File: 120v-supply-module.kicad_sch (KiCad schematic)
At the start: 10 parts

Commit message: Place Holder:
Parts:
- removed U?: (no value), symbol Sensor_Current:ACS706xLC-05C
- added SW2: SW_DP3T, symbol Switch:SW_DP3T
- F2: value (none) -> Fuse
- J1: renamed from J?; value (none) -> VAC_GROUND_TERM
- J3: value (none) -> VAC_LIVE_TERM
- J4: value (none) -> VAC_NUETRAL_TERM
- K2: value (none) -> 12VDC SPDT Relay (240V 10A); footprint (none) -> Relay_THT:Relay_SPDT_RAYEX-L90S
- SW3: value (none) -> SW_SP3T
- SW4: value (none) -> SW_SPST
- T1: value (none) -> Transformer_1P_1S
- U1: value (none) -> AC PWM; footprint (none) -> Package_SO:SOIC-8_3.9x4.9mm_P1.27mm
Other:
- note added: "AC PWM Device"
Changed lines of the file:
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@@
     (effects (font (size 1.27 1.27)) (justify left bottom))
   )
-  (text "NOTE: ALL VAC IS UNPROTECTED BY THE POWER SUPPLY." (at 115.57 52.07 0)
+  (text "NOTE: ALL VAC IS UNPROTECTED BY THE POWER SUPPLY." (at 35.56 39.37 0)
     (effects (font (size 1.27 1.27) (thickness 0.254) bold) (justify left bottom))
   )
@@
     (effects (font (size 1.27 1.27)) (justify left bottom))
   )
-  (text "VAC_NUETRAL" (at 49.53 134.62 0)
+  (text "VAC_NUETRAL" (at 45.72 134.62 0)
     (effects (font (size 1.27 1.27)) (justify left bottom))
   )
@@
     (effects (font (size 1.27 1.27)) (justify left bottom))
   )
+  (text "AC PWM Device" (at 72.39 99.06 0)
+    (effects (font (size 1.27 1.27)) (justify left bottom))
+  )
   (text "120VAC_DIRECT_SUPPLY" (at 82.55 78.74 0)
     (effects (font (size 1.27 1.27)) (justify left bottom))
@@
       (effects (font (size 1.27 1.27)) (justify right))
     )
-    (property "Value" "" (id 1) (at 88.9 105.4099 0)
+    (property "Value" "AC PWM " (id 1) (at 88.9 105.4099 0)
       (effects (font (size 1.27 1.27)) (justify right))
     )
-    (property "Footprint" "" (id 2) (at 88.9 106.68 0)
+    (property "Footprint" "Package_SO:SOIC-8_3.9x4.9mm_P1.27mm" (id 2) (at 88.9 106.68 0)
       (effects (font (size 1.27 1.27) italic) (justify left) hide)
     )
@@
     (in_bom yes) (on_board yes) (fields_autoplaced)
     (property "Reference" "T1" (id 0) (at 72.4027 120.65 0))
-    (property "Value" "" (id 1) (at 72.4027 123.19 0))
+    (property "Value" "Transformer_1P_1S" (id 1) (at 72.4027 123.19 0))
     (property "Footprint" "" (id 2) (at 72.39 130.81 0)
       (effects (font (size 1.27 1.27)) hide)
@@
       (effects (font (size 1.27 1.27)) (justify left))
     )
-    (property "Value" "" (id 1) (at 205.74 100.3299 0)
+    (property "Value" "12VDC SPDT Relay (240V 10A)" (id 1) (at 205.74 100.3299 0)
       (effects (font (size 1.27 1.27)) (justify left))
     )
-    (property "Footprint" "" (id 2) (at 205.74 100.33 0)
+    (property "Footprint" "Relay_THT:Relay_SPDT_RAYEX-L90S" (id 2) (at 205.74 100.33 0)
       (effects (font (size 1.27 1.27)) (justify left) hide)
     )
@@
     (in_bom yes) (on_board yes)
     (property "Reference" "J3" (id 0) (at 28.575 73.66 0))
-    (property "Value" "" (id 1) (at 28.575 76.2 0))
+    (property "Value" "VAC_LIVE_TERM" (id 1) (at 28.575 76.2 0))
     (property "Footprint" "" (id 2) (at 27.94 78.74 0)
       (effects (font (size 1.27 1.27)) hide)
@@
     (pin "1")
   )
-  (symbol (lib_id "Switch:SW_SPST") (at 226.06 81.28 0) (unit 1)
-    (in_bom yes) (on_board yes) (fields_autoplaced)
-    (property "Reference" "SW4" (id 0) (at 226.06 74.93 0))
-    (property "Value" "" (id 1) (at 226.06 77.47 0))
-    (property "Footprint" "" (id 2) (at 226.06 81.28 0)
-      (effects (font (size 1.27 1.27)) hide)
-    )
-    (property "Datasheet" "~" (id 3) (at 226.06 81.28 0)
-      (effects (font (size 1.27 1.27)) hide)
-    )
-    (pin "1")
-    (pin "2")
-  )
-  (symbol (lib_id "Connector:Conn_01x01_Male") (at 27.94 156.21 0) (unit 1)
-    (in_bom yes) (on_board yes)
-    (property "Reference" "J4" (id 0) (at 27.94 158.75 0))
-    (property "Value" "" (id 1) (at 28.575 153.67 0))
-    (property "Footprint" "" (id 2) (at 27.94 156.21 0)
-      (effects (font (size 1.27 1.27)) hide)
-    )
-    (property "Datasheet" "~" (id 3) (at 27.94 156.21 0)
-      (effects (font (size 1.27 1.27)) hide)
-    )
-    (pin "1")
-  )
-  (symbol (lib_id "Switch:SW_SP3T") (at 116.84 81.28 0) (mirror y) (unit 1)
-    (in_bom yes) (on_board yes) (fields_autoplaced)
-    (property "Reference" "SW3" (id 0) (at 116.84 73.66 0))
-    (property "Value" "" (id 1) (at 116.84 76.2 0))
-    (property "Footprint" "" (id 2) (at 132.715 76.835 0)
-      (effects (font (size 1.27 1.27)) hide)
-    )
-    (property "Datasheet" "~" (id 3) (at 132.715 76.835 0)
-      (effects (font (size 1.27 1.27)) hide)
-    )
-    (pin "1")
-    (pin "2")
-    (pin "3")
-    (pin "4")
-  )
-  (symbol (lib_id "Connector:Conn_01x01_Male") (at 27.94 167.64 0) (unit 1)
-    (in_bom yes) (on_board yes)
-    (property "Reference" "J?" (id 0) (at 27.94 170.18 0))
-    (property "Value" "" (id 1) (at 28.575 165.1 0))
-    (property "Footprint" "" (id 2) (at 27.94 167.64 0)
-      (effects (font (size 1.27 1.27)) hide)
-    )
-    (property "Datasheet" "~" (id 3) (at 27.94 167.64 0)
-      (effects (font (size 1.27 1.27)) hide)
-    )
-    (pin "1")
-  )
-  (symbol (lib_id "Device:Fuse") (at 158.75 81.28 90) (mirror x) (unit 1)
-    (in_bom yes) (on_board yes) (fields_autoplaced)
-    (property "Reference" "F2" (id 0) (at 158.75 74.93 90))
-    (property "Value" "" (id 1) (at 158.75 77.47 90))
-    (property "Footprint" "" (id 2) (at 158.75 79.502 90)
-      (effects (font (size 1.27 1.27)) hide)
-    )
-    (property "Datasheet" "~" (id 3) (at 158.75 81.28 0)
-      (effects (font (size 1.27 1.27)) hide)
-    )
-    (pin "1")
-    (pin "2")
-  )
-  (symbol (lib_id "Sensor_Current:ACS706xLC-05C") (at 81.28 59.69 0) (mirror y) (unit 1)
-    (in_bom yes) (on_board yes) (fields_autoplaced)
-    (property "Reference" "U?" (id 0) (at 72.39 58.4199 0)
-      (effects (font (size 1.27 1.27)) (justify right))
-    )
-    (property "Value" "" (id 1) (at 72.39 60.9599 0)
-      (effects (font (size 1.27 1.27)) (justify right))
-    )
-    (property "Footprint" "" (id 2) (at 72.39 62.23 0)
-      (effects (font (size 1.27 1.27) italic) (justify left) hide)
-    )
-    (property "Datasheet" "http://www.allegromicro.com/~/media/Files/Datasheets/ACS706ELC-05C-Datasheet.ashx" (id 3) (at 81.28 59.69 0)
+  (symbol (lib_id "Switch:SW_DP3T") (at 121.92 38.1 0) (unit 2)
+    (in_bom yes) (on_board yes) (fields_autoplaced)
+    (property "Reference" "SW2" (id 0) (at 121.92 30.48 0))
+    (property "Value" "SW_DP3T" (id 1) (at 121.92 33.02 0))
+    (property "Footprint" "" (id 2) (at 106.045 33.655 0)
+      (effects (font (size 1.27 1.27)) hide)
+    )
+    (property "Datasheet" "~" (id 3) (at 106.045 33.655 0)
       (effects (font (size 1.27 1.27)) hide)
     )
@@
     (pin "8")
   )
+  (symbol (lib_id "Switch:SW_DP3T") (at 109.22 38.1 0) (unit 1)
+    (in_bom yes) (on_board yes) (fields_autoplaced)
+    (property "Reference" "SW2" (id 0) (at 109.22 30.48 0))
+    (property "Value" "SW_DP3T" (id 1) (at 109.22 33.02 0))
+    (property "Footprint" "" (id 2) (at 93.345 33.655 0)
+      (effects (font (size 1.27 1.27)) hide)
+    )
+    (property "Datasheet" "~" (id 3) (at 93.345 33.655 0)
+      (effects (font (size 1.27 1.27)) hide)
+    )
+    (pin "1")
+    (pin "2")
+    (pin "3")
+    (pin "4")
+    (pin "5")
+    (pin "6")
+    (pin "7")
+    (pin "8")
+  )
+  (symbol (lib_id "Switch:SW_SPST") (at 226.06 81.28 0) (unit 1)
+    (in_bom yes) (on_board yes) (fields_autoplaced)
+    (property "Reference" "SW4" (id 0) (at 226.06 74.93 0))
+    (property "Value" "SW_SPST" (id 1) (at 226.06 77.47 0))
+    (property "Footprint" "" (id 2) (at 226.06 81.28 0)
+      (effects (font (size 1.27 1.27)) hide)
+    )
+    (property "Datasheet" "~" (id 3) (at 226.06 81.28 0)
+      (effects (font (size 1.27 1.27)) hide)
+    )
+    (pin "1")
+    (pin "2")
+  )
+  (symbol (lib_id "Connector:Conn_01x01_Male") (at 27.94 156.21 0) (unit 1)
+    (in_bom yes) (on_board yes)
+    (property "Reference" "J4" (id 0) (at 27.94 158.75 0))
+    (property "Value" "VAC_NUETRAL_TERM" (id 1) (at 28.575 153.67 0))
+    (property "Footprint" "" (id 2) (at 27.94 156.21 0)
+      (effects (font (size 1.27 1.27)) hide)
+    )
+    (property "Datasheet" "~" (id 3) (at 27.94 156.21 0)
+      (effects (font (size 1.27 1.27)) hide)
+    )
+    (pin "1")
+  )
+  (symbol (lib_id "Switch:SW_SP3T") (at 116.84 81.28 0) (mirror y) (unit 1)
+    (in_bom yes) (on_board yes) (fields_autoplaced)
+    (property "Reference" "SW3" (id 0) (at 116.84 73.66 0))
+    (property "Value" "SW_SP3T" (id 1) (at 116.84 76.2 0))
+    (property "Footprint" "" (id 2) (at 132.715 76.835 0)
+      (effects (font (size 1.27 1.27)) hide)
+    )
+    (property "Datasheet" "~" (id 3) (at 132.715 76.835 0)
+      (effects (font (size 1.27 1.27)) hide)
+    )
+    (pin "1")
+    (pin "2")
+    (pin "3")
+    (pin "4")
+  )
+  (symbol (lib_id "Connector:Conn_01x01_Male") (at 27.94 167.64 0) (unit 1)
+    (in_bom yes) (on_board yes)
+    (property "Reference" "J1" (id 0) (at 27.94 170.18 0))
+    (property "Value" "VAC_GROUND_TERM" (id 1) (at 28.575 165.1 0))
+    (property "Footprint" "" (id 2) (at 27.94 167.64 0)
+      (effects (font (size 1.27 1.27)) hide)
+    )
+    (property "Datasheet" "~" (id 3) (at 27.94 167.64 0)
+      (effects (font (size 1.27 1.27)) hide)
+    )
+    (pin "1")
+  )
+  (symbol (lib_id "Device:Fuse") (at 158.75 81.28 90) (mirror x) (unit 1)
+    (in_bom yes) (on_board yes) (fields_autoplaced)
+    (property "Reference" "F2" (id 0) (at 158.75 74.93 90))
+    (property "Value" "Fuse" (id 1) (at 158.75 77.47 90))
+    (property "Footprint" "" (id 2) (at 158.75 79.502 90)
+      (effects (font (size 1.27 1.27)) hide)
+    )
+    (property "Datasheet" "~" (id 3) (at 158.75 81.28 0)
+      (effects (font (size 1.27 1.27)) hide)
+    )
+    (pin "1")
+    (pin "2")
+  )
 )

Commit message: Draft 5VDC Supply Schematic
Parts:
- removed F2: Fuse, symbol Device:Fuse
- removed J1: VAC_GROUND_TERM, symbol Connector:Conn_01x01_Male
- removed J3: VAC_LIVE_TERM, symbol Connector:Conn_01x01_Male
- removed J4: VAC_NUETRAL_TERM, symbol Connector:Conn_01x01_Male
- removed K2: 12VDC SPDT Relay (240V 10A), Relay_THT:Relay_SPDT_RAYEX-L90S, symbol Relay:RAYEX-L90S
- removed SW2: SW_DP3T, symbol Switch:SW_DP3T
- removed SW3: SW_SP3T, symbol Switch:SW_SP3T
- removed SW4: SW_SPST, symbol Switch:SW_SPST
- removed U1: AC PWM, Package_SO:SOIC-8_3.9x4.9mm_P1.27mm, symbol Sensor_Current:ACS706xLC-05C
- added F? (x2): Fuse, symbol Device:Fuse
- added J? (x3): Conn_01x01_MountingPin, symbol Connector_Generic_MountingPin:Conn_01x01_MountingPin
- added K?: 12VDC SPDT Relay (240V 10A), Relay_THT:Relay_SPDT_RAYEX-L90S, symbol Relay:RAYEX-L90S
- added M?: 4_Pin_Meter_With_Toroid, symbol bvm-library:4_Pin_Meter_With_Toroid
- added SW?: SW_Rotary2x6, symbol Switch:SW_Rotary2x6
- added SW_AC_MODULE: SW_SPST_LED, symbol Switch:SW_SPST_LED
- added T?: 1000/1 10Ω, symbol bvm-library:Open_Half_Loop_Toroidal_Current_Sensor
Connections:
- net at T1.1 (AA): now also SW?.3
- net VAC_L: now reaches T1.2 (AB)
- net VAC_L: now also SW?.8, SW?.9
- net VAC_L_OUT: now reaches T1.3 (SA)
- net VAC_L_OUT: now also J?.1 (Pin_1), SW?.7
- net VAC_N_OUT: now reaches T1.4 (SB)
- net VAC_N_OUT: now also J?.1 (Pin_1), SW?.1, SW?.2
- new net: M?.3 (Coil+), T?.1 (Current_Sense_A)
- new net: M?.4 (Coil-), T?.2 (Current_Sense_B)
- new net: K?.12, SW_AC_MODULE.2, SW_AC_MODULE.4 (A)
- new net: F?.2, K?.A2, M?.1 (L)
- new net 120VAC_FUSED_L: F?.1, SW?.14
- new net 120VAC_FUSED_N: F?.1, SW?.13
- new net 120VAC_SUPPLY_L: K?.A1
- new net 120VAC_SUPPLY_N: F?.2, M?.2 (N)
- new net 12VDC_SUPPLY: SW_AC_MODULE.1
- new net VAC_GROUND: J?.1 (Pin_1)
- new net VDC_GND: K?.11, SW_AC_MODULE.3 (K)
- no-connect marks 1 -> 6
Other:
- note added: "120VAC_FUSED_L"
- note added: "AC PWM Driver"
- note added: "Is the fuse on 120VAC_FUSED_N necessary?"
- note removed: "120V VARIAC_SUPPLY"
- note removed: "120VAC DRIVER SUPPLY"
- note removed: "120VAC Supply Module"
- note removed: "120VAC_AC_ZONE_SUPPLY"
- note removed: "120VAC_DIRECT_SUPPLY"
- note removed: "120VAC_NUETRAL"
- note removed: "120VAC_SUPPLY"
- note removed: "12VDC_CONTROL_SUPPLY"
- note removed: "12VDC_VADC_ZONE_CONTROL"
- note removed: "AC PWM Device"
- note removed: "VAC_GROUND"
- note removed: "VAC_LIVE"
- note removed: "VAC_NUETRAL"
- moved on the sheet: T1

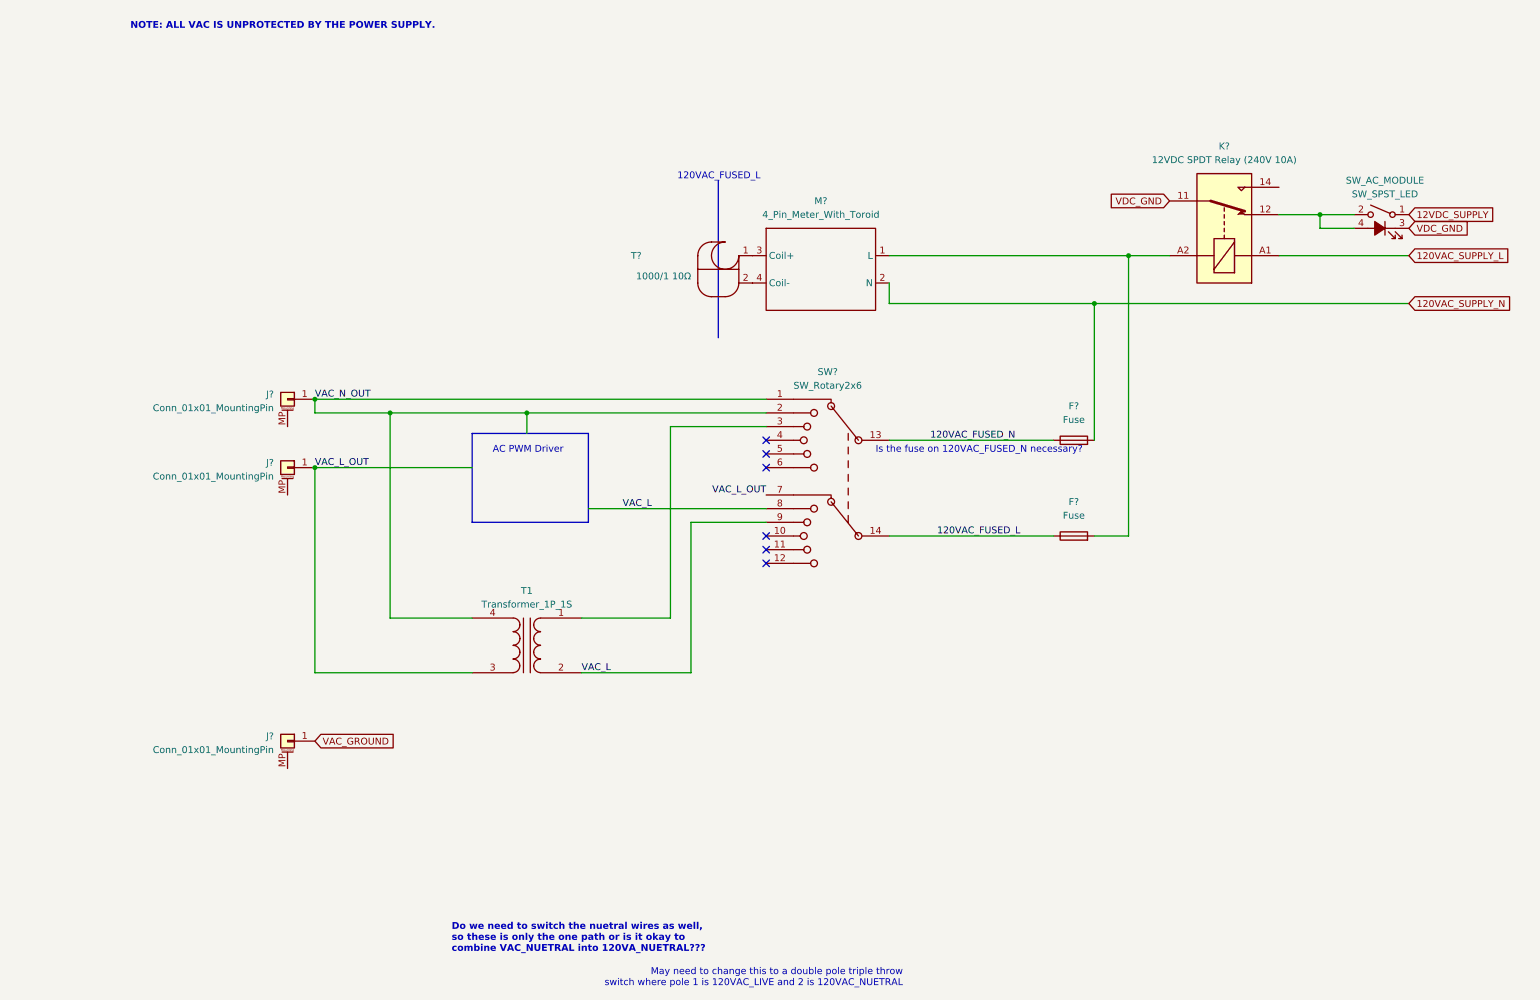
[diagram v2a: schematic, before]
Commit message: Save more changes
Started Fan Control
Created VDC Meter Template
Fleshed out 12, 5, 5-usb, and 3.3 modules
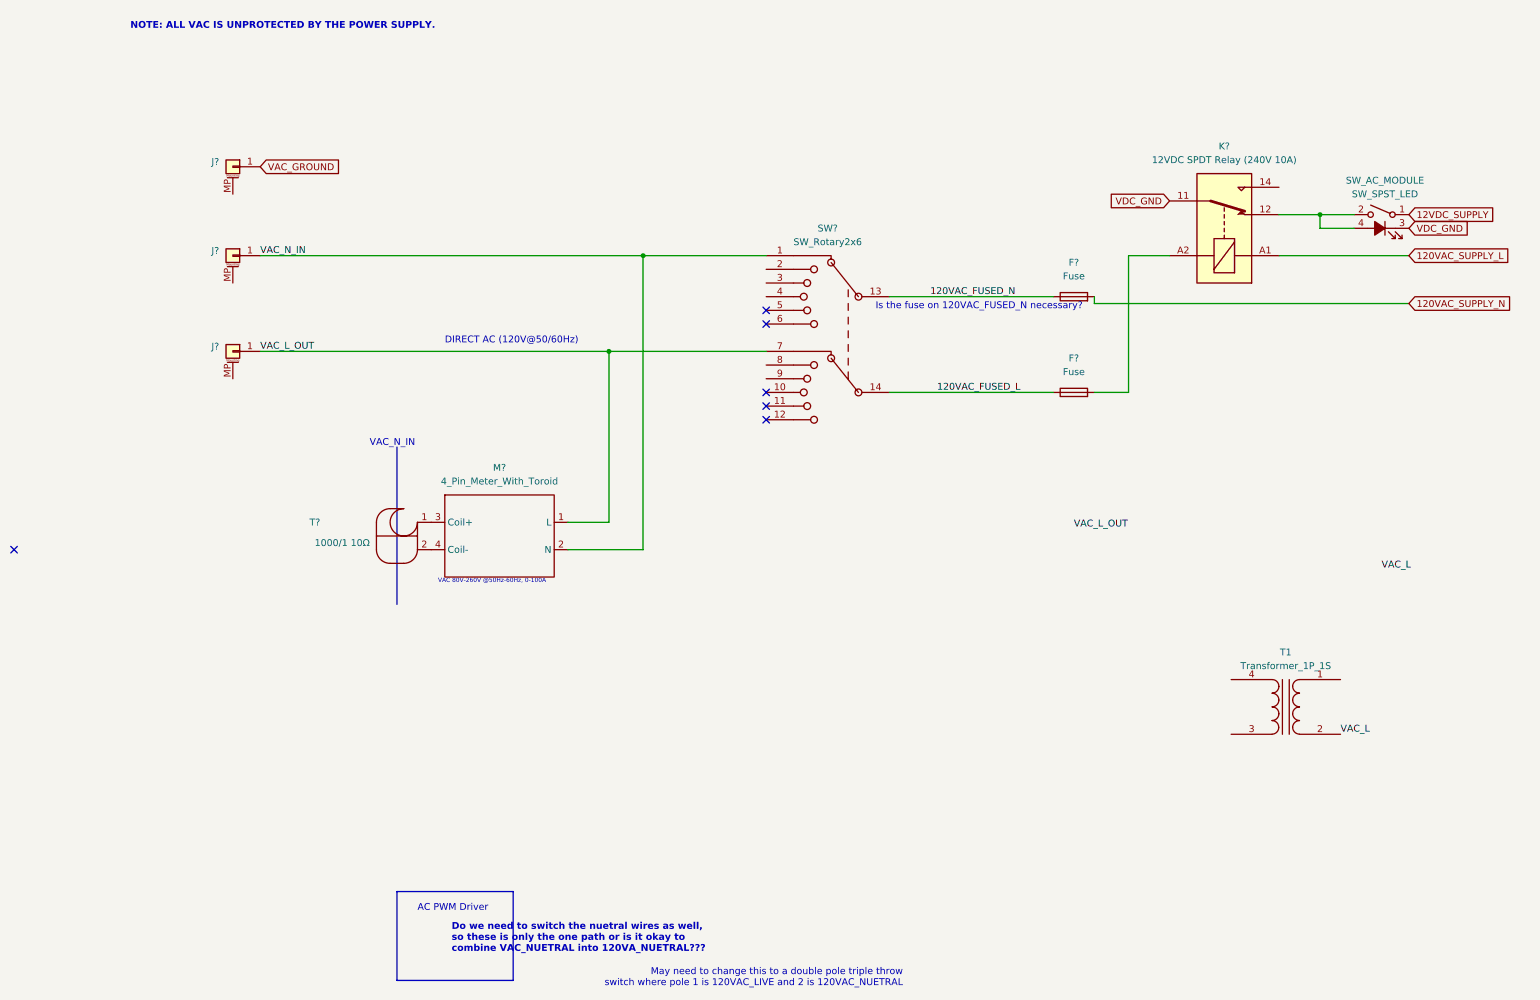
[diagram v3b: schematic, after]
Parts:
- removed J? (x2): Conn_01x01_MountingPin, symbol Connector_Generic_MountingPin:Conn_01x01_MountingPin
- added J? (x2): (no value), symbol Connector_Generic_MountingPin:Conn_01x01_MountingPin
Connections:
- net 120VAC_SUPPLY_N: no longer M?.2 (N)
- net VAC_L: no longer SW?.8, SW?.9
- net VAC_L_OUT: now also M?.1 (L), J?.1 (Pin_1); no longer T1.3 (SA)
- net at T1.1 (AA): no longer SW?.3
- net at F?.2, K?.A2: no longer M?.1 (L)
- removed net VAC_N_OUT: SW?.1, SW?.2, T1.4 (SB)
- new net VAC_N_IN: J?.1 (Pin_1), M?.2 (N), SW?.1
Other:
- note added: "DIRECT AC (120V@50/60Hz)"
- note added: "VAC 80V-260V @50Hz-60Hz, 0-100A"
- note added: "VAC_N_IN"
- note removed: "120VAC_FUSED_L"
- moved on the sheet: F?, J?, M?, SW?, T1, T?

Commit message: Bunch more changes
Blah blah
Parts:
- removed F?: Fuse, symbol Device:Fuse
- added U?: 100A_AC_PWM_Driver, symbol bvm-library:100A_AC_PWM_Driver
- F?: value Fuse -> 10A
- J? (x2): value (none) -> Conn_01x01_MountingPin
- M?: value 4_Pin_Meter_With_Toroid -> PZEM-022
- gave numbers to parts that had none: 1
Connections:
- net 120VAC_FUSED_N is gone; now on net 120VAC_SUPPLY_N: SW_AC_DRIVE.13
- net VAC_L is gone; now on net VAC_TRANS_L_IN: T1.2 (AB)
- net VAC_GROUND: now also U?.1 (OUT)
- net VAC_L_OUT: now also T1.3 (SA), U?.1 (OUT); no longer J?.1 (Pin_1)
- net VAC_N_IN: now also SW_AC_DRIVE.2, T1.4 (SB)
- net VAC_TRANS_N_OUT: now reaches T1.1 (AA)
- net VAC_DRIVE_L_IN: now reaches SW_AC_DRIVE.8
- net VAC_DRIVE_L_IN: now also U?.1 (OUT)
- net VAC_TRANS_L_IN: now reaches SW_AC_DRIVE.9
- no-connect marks 6 -> 7
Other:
- note added: "Position 1: DIRECT AC (120V@50/60Hz) Position 2: PWM AC Position 3: VARIAC AC"
- note removed: "AC PWM Driver"
- note removed: "DIRECT AC (120V@50/60Hz)"
- note removed: "Do we need to switch the nuetral wires as well, so these is only the one path or is it okay to combine VAC_NUETRAL into 120VA_NUETRAL???"
- note removed: "Is the fuse on 120VAC_FUSED_N necessary?"
- note removed: "May need to change this to a double pole triple throw switch where pole 1 is 120VAC_LIVE and 2 is 120VAC_NUETRAL"
- title: 120V AC Module -> Mr. Powers
- moved on the sheet: F?, J?, K?, M?, SW_AC_DRIVE, SW_AC_MODULE, T1, T?

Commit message: Minor change across the board
I need better notes.
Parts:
- removed J? (x3): Conn_01x01_MountingPin, symbol Connector_Generic_MountingPin:Conn_01x01_MountingPin
- added D3, D4: D, symbol Device:D
- added J11: Screw_Terminal_01x03, symbol Connector:Screw_Terminal_01x03
- gave numbers to parts that had none: 5
- renumbered SW_AC_DRIVE to SW_AC_DRIVE1, SW_AC_MODULE to SW_AC_MODULE1
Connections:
- net VAC_DRIVE_L_IN: now also U1.2 (IN); no longer SW_AC_DRIVE1.8, U1.1 (OUT)
- net VAC_GROUND: now also U1.3 (COM), J11.3 (Pin_3); no longer U1.1 (OUT)
- net VAC_L_OUT: now also D3.1 (K), D3.2 (A), D4.1 (K), J11.2 (Pin_2); no longer U1.1 (OUT)
- net VAC_N_IN: now also J11.1 (Pin_1)
- net VAC_TRANS_N_OUT: now also SW_AC_DRIVE1.3
- net 120VAC_SUPPLY_L renamed 120VAC_INT_SUPPLY_L
- new net: D4.2 (A), U1.1 (OUT)
- no-connect marks 7 -> 6
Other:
- moved on the sheet: F_120VAC_1, T1, U1
